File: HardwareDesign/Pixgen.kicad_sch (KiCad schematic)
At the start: 11 parts, among them U601 GAL22V10, U602 74HCT574, U603 27SF512, U604 74HCT574, U605 GAL22V10

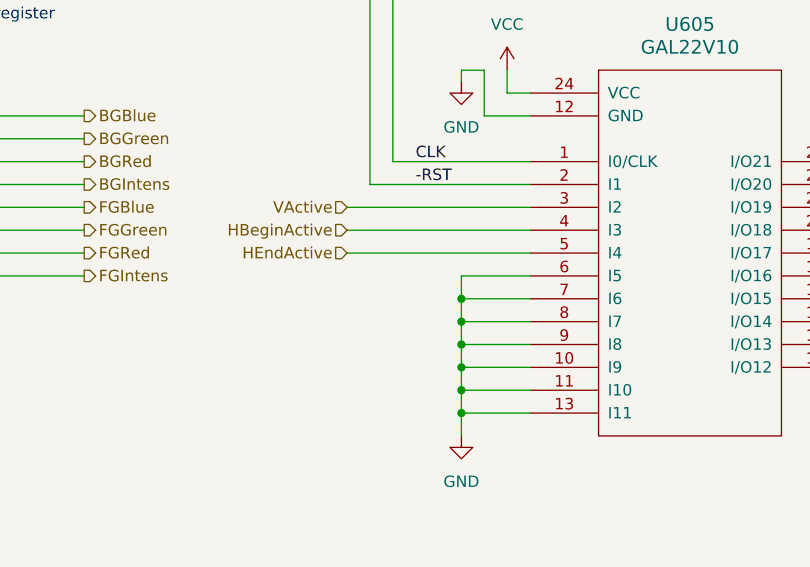
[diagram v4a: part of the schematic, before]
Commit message: updated schematic to send -VIS to Pixgen module
The Pixgen module should only shift data in the output
shift register if a visible pixel is being displayed.

Also, change Pixgen control GAL equations and simulation
to reflect -VIS being an active-low signal (they were
previously representing it as an active-high signal.)
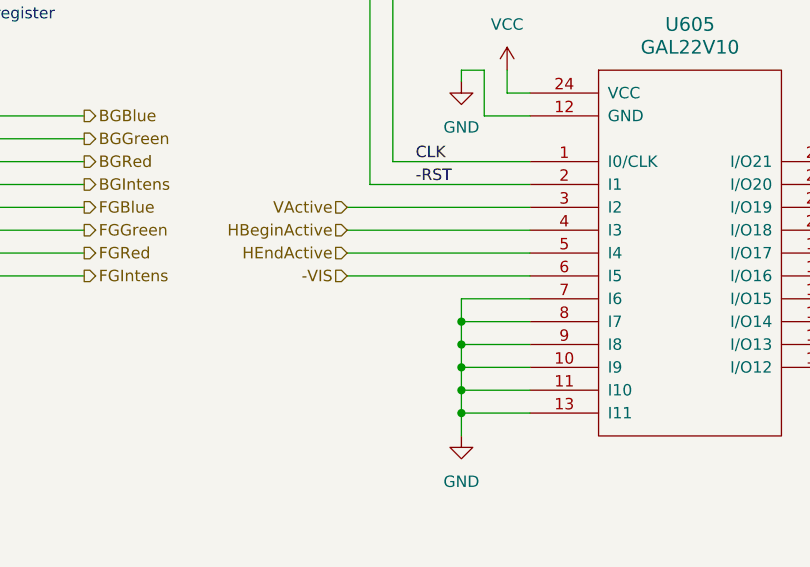
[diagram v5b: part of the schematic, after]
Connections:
- net GND: no longer U605.6 (I5)
- new net -VIS: U605.6 (I5)
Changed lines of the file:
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@@
 		(color 0 0 0 0)
 	)
-	(junction
-		(at 128.27 144.78)
-		(diameter 0)
-		(color 0 0 0 0)
-	)
 	(bus_entry
 		(at 100.33 48.26)
@@
 		)
 	)
-	(wire
-		(pts
-			(xy 128.27 142.24) (xy 128.27 144.78)
-		)
-		(stroke
-			(width 0)
-			(type default)
-		)
-	)
 	(bus
 		(pts
@@
 	(wire
 		(pts
+			(xy 115.57 142.24) (xy 135.89 142.24)
+		)
+		(stroke
+			(width 0)
+			(type default)
+		)
+	)
+	(wire
+		(pts
 			(xy 91.44 40.64) (xy 100.33 40.64)
 		)
@@
 		)
 	)
-	(wire
-		(pts
-			(xy 135.89 142.24) (xy 128.27 142.24)
-		)
-		(stroke
-			(width 0)
-			(type default)
-		)
-	)
 	(bus
 		(pts
@@
 		(fields_autoplaced yes)
 		(effects
+			(font
+				(size 1.27 1.27)
+			)
+			(justify right)
+		)
+	)
+	(hierarchical_label "-VIS"
+		(shape input)
+		(at 115.57 142.24 180)
+		(fields_autoplaced yes)
+		(effects

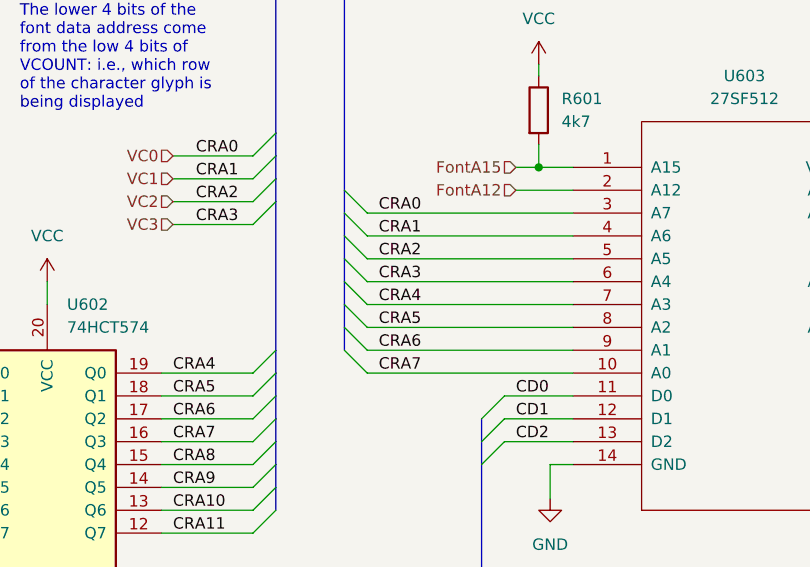
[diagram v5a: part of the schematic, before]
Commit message: fix font ROM address input signals
I had bits 0-7 connected in reverse previously.
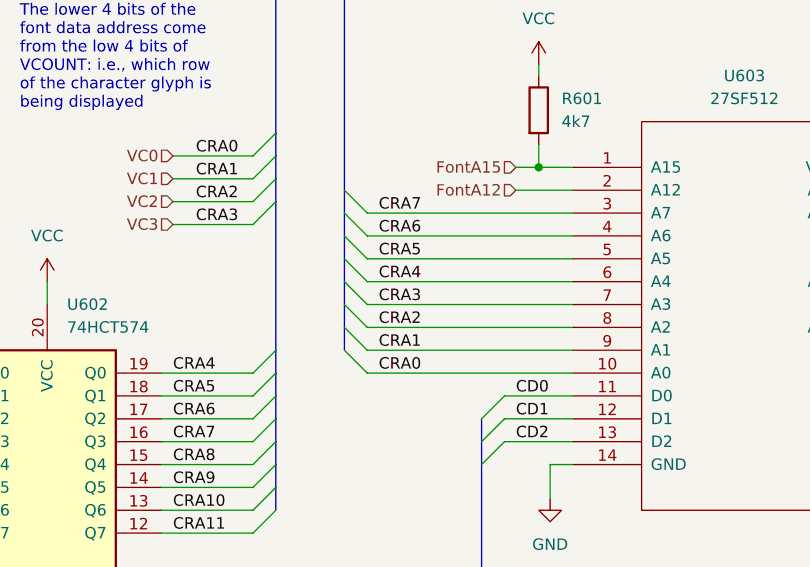
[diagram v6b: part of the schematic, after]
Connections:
- net CRA4: now also U603.6 (A4); no longer U603.7 (A3)
- net CRA5: now also U603.5 (A5); no longer U603.8 (A2)
- net CRA6: now also U603.4 (A6); no longer U603.9 (A1)
- net CRA7: now also U603.3 (A7); no longer U603.10 (A0)
- net VC0: now also U603.10 (A0); no longer U603.3 (A7)
- net VC1: now also U603.9 (A1); no longer U603.4 (A6)
- net VC2: now also U603.8 (A2); no longer U603.5 (A5)
- net VC3: now also U603.7 (A3); no longer U603.6 (A4)
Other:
- title: Pixel generation -> Pixel generator
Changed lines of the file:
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@@
 	(paper "USLetter")
 	(title_block
-		(title "Pixel generation")
+		(title "Pixel generator")
 		(company "daveho hacks")
 	)
@@
 	)
 	(label "CRA5"
-		(at 114.3 59.69 0)
+		(at 114.3 52.07 0)
 		(fields_autoplaced yes)
 		(effects
@@
 	)
 	(label "CRA6"
-		(at 114.3 62.23 0)
+		(at 114.3 49.53 0)
 		(fields_autoplaced yes)
 		(effects
@@
 	)
 	(label "CRA3"
-		(at 114.3 54.61 0)
+		(at 114.3 57.15 0)
 		(fields_autoplaced yes)
 		(effects
@@
 	)
 	(label "CRA4"
-		(at 114.3 57.15 0)
+		(at 114.3 54.61 0)
 		(fields_autoplaced yes)
 		(effects
@@
 	)
 	(label "CRA1"
-		(at 114.3 49.53 0)
+		(at 114.3 62.23 0)
 		(fields_autoplaced yes)
 		(effects
@@
 	)
 	(label "CRA2"
-		(at 114.3 52.07 0)
+		(at 114.3 59.69 0)
 		(fields_autoplaced yes)
 		(effects
@@
 	)
 	(label "CRA7"
-		(at 114.3 64.77 0)
+		(at 114.3 46.99 0)
 		(fields_autoplaced yes)
 		(effects
@@
 	)
 	(label "CRA0"
-		(at 114.3 46.99 0)
+		(at 114.3 64.77 0)
 		(fields_autoplaced yes)
 		(effects

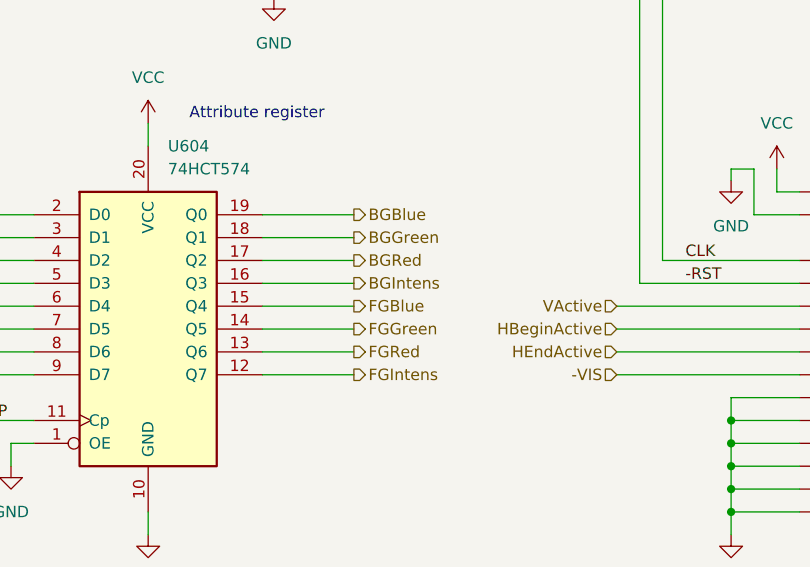
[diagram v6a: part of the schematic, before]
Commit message: fix attribute register outputs
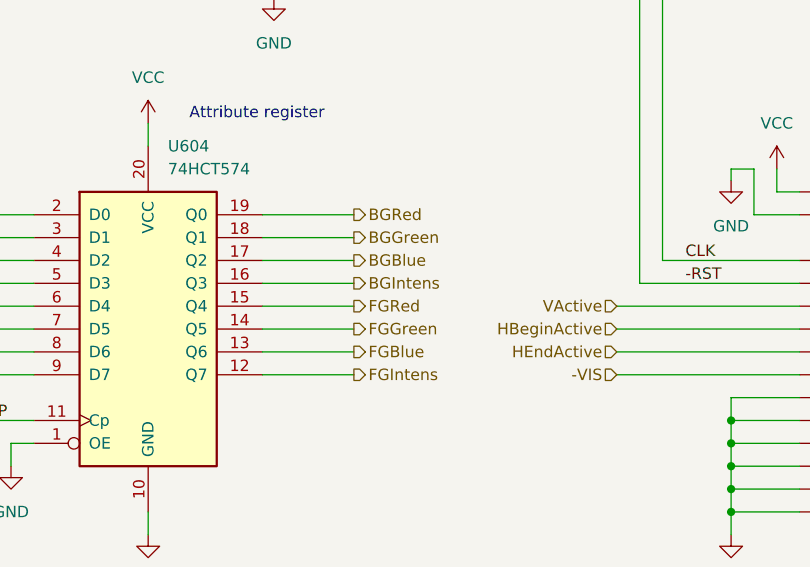
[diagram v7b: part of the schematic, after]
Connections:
- net BGBlue: now also U604.17 (Q2); no longer U604.19 (Q0)
- net BGRed: now also U604.19 (Q0); no longer U604.17 (Q2)
- net FGBlue: now also U604.13 (Q6); no longer U604.15 (Q4)
- net FGRed: now also U604.15 (Q4); no longer U604.13 (Q6)

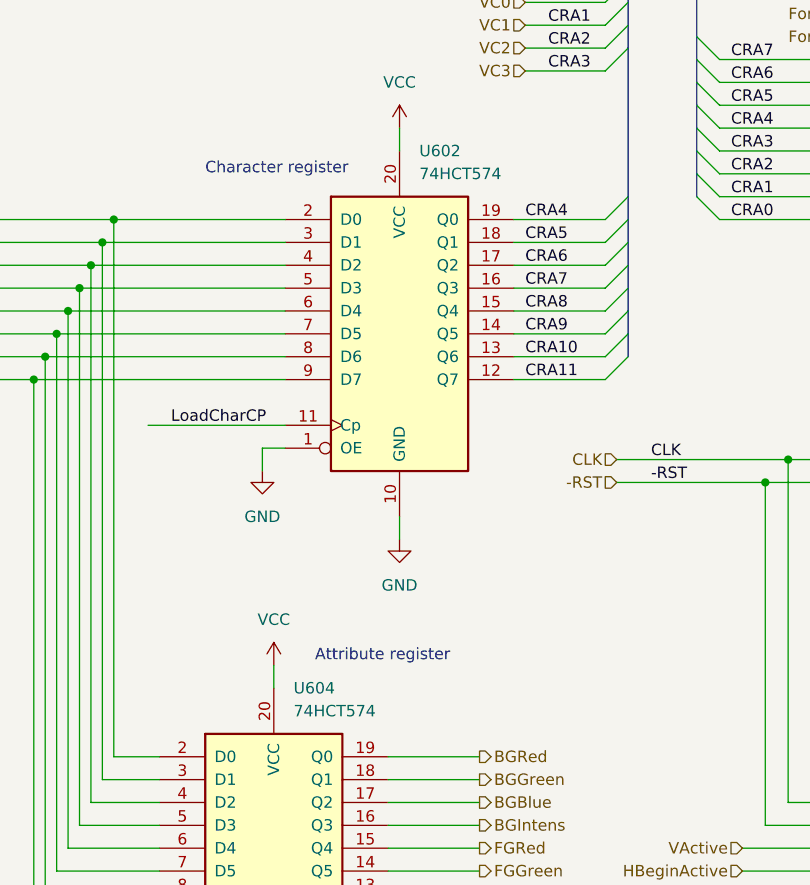
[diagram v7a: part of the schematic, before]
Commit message: use 74ALS and 74HCT parts where possible
The '574 implementing the VRAM module's bank register
can be a 74HCT574 because it's only driven by
(relatively slow) signals from the host system.

Changed the Readout module to use 74ALS273 rather than
74ACT273 for the row begin address register.

Changed the Pixgen module to use 74ALS574 rather than
74ACT574 for the character and attribute registers.
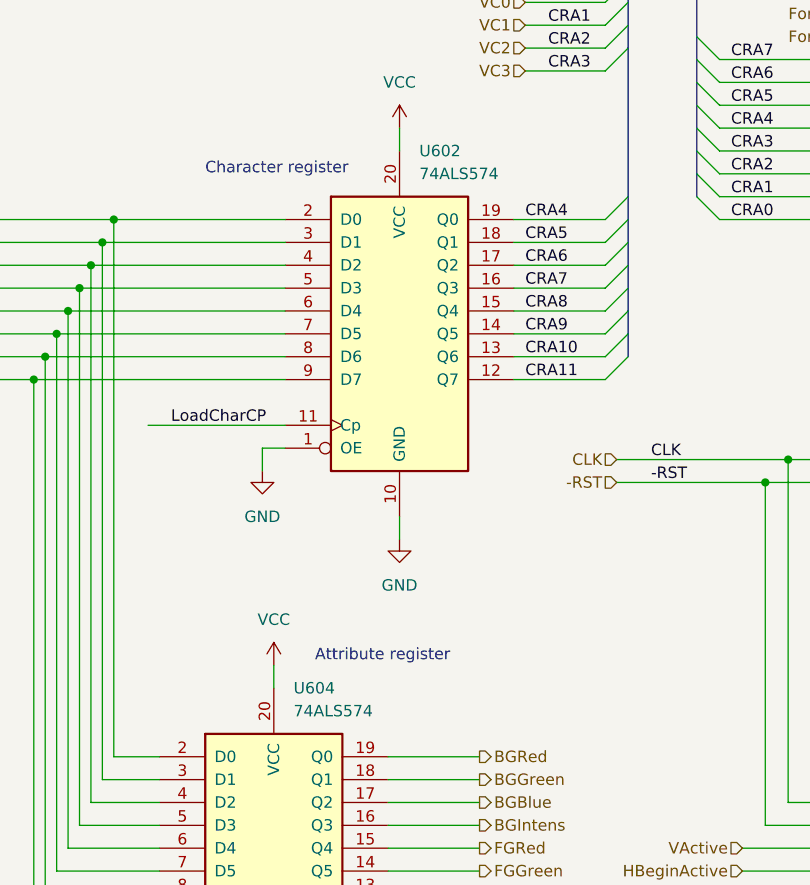
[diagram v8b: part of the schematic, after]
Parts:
- U602, U604: value 74HCT574 -> 74ALS574
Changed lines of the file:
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@@
 			)
 		)
-		(property "Value" "74HCT574"
+		(property "Value" "74ALS574"
 			(at 79.6641 59.69 0)
 			(effects
@@
 			)
 		)
-		(property "Value" "74HCT574"
+		(property "Value" "74ALS574"
 			(at 65.6941 119.38 0)
 			(effects
